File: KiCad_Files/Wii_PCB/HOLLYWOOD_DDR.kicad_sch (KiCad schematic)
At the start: 1 part

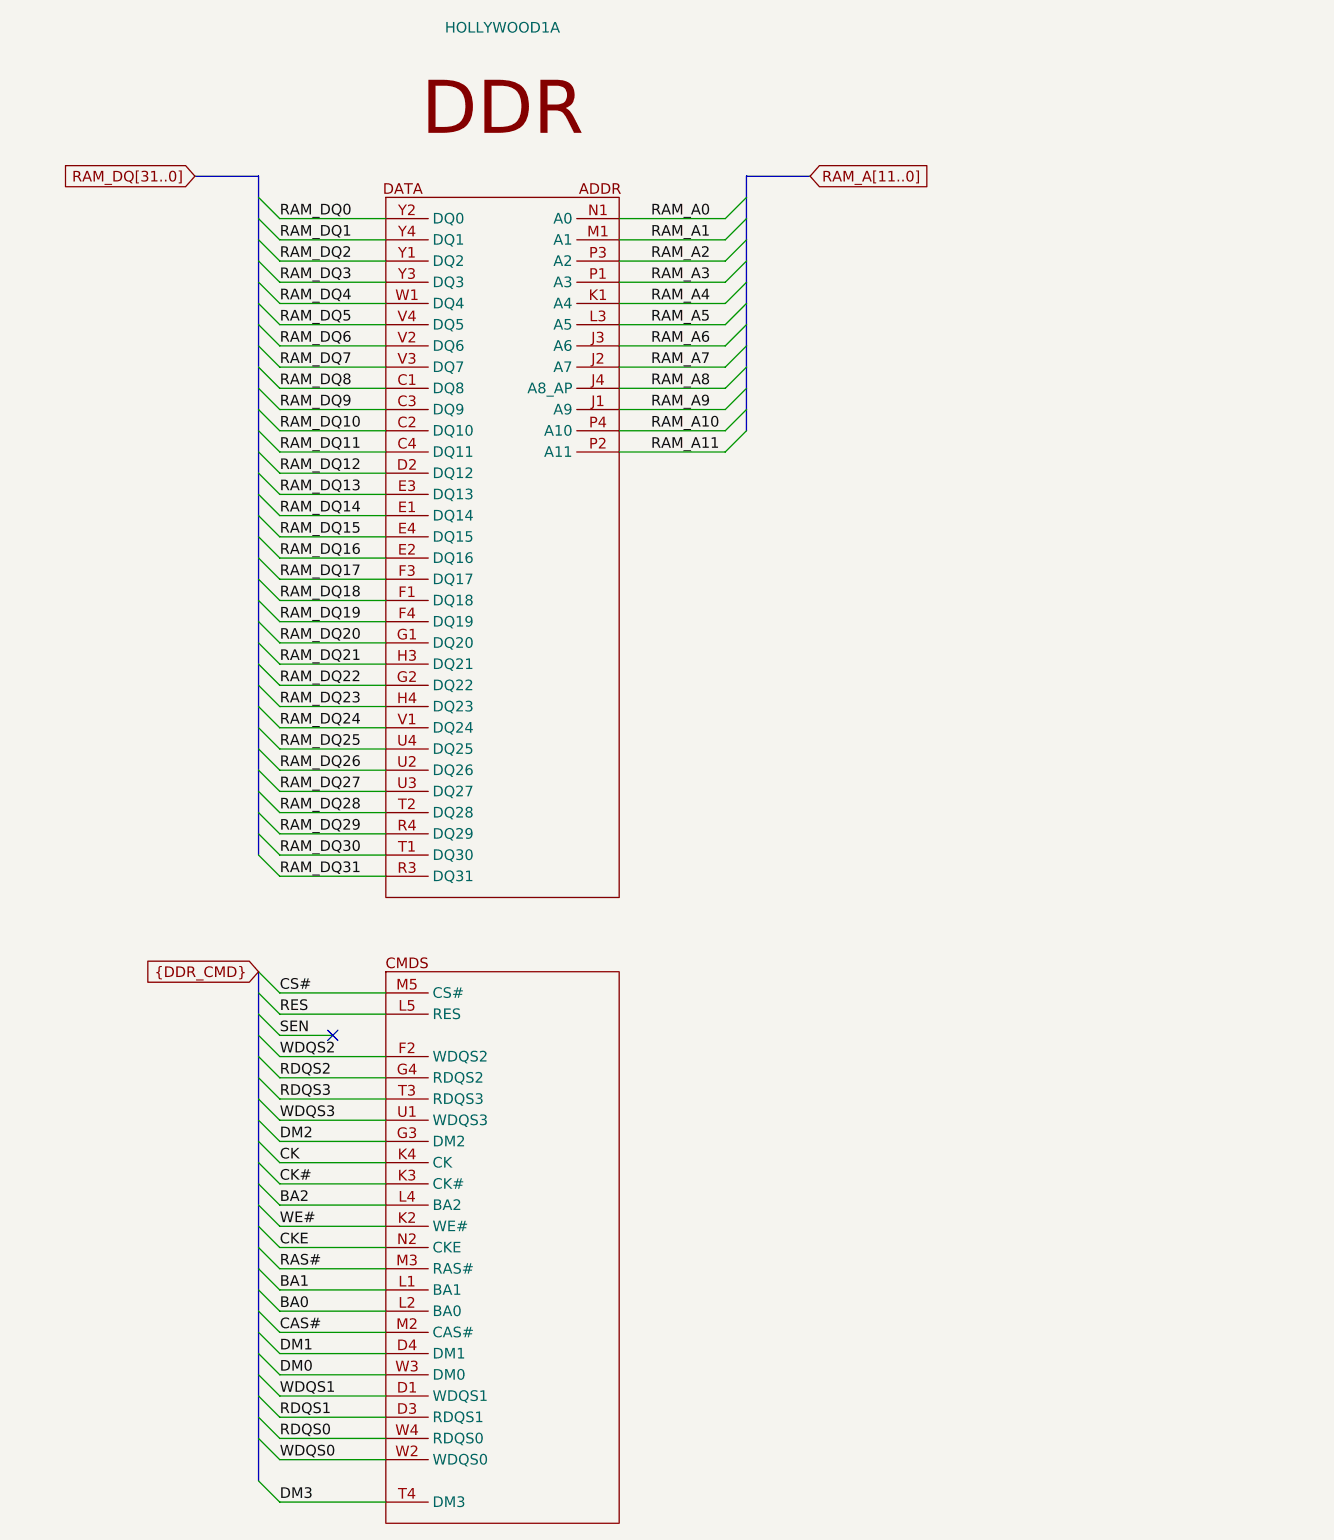
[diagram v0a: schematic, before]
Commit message: Updated RAM & GPU bus to allow custom net rules for measuring intra-track spacing, added pad for reset, removed debug pads, reorganized ram schematic to cluster length matched signals, changed MX chip and U10 symbols, and re-labeled the wifi net interface.
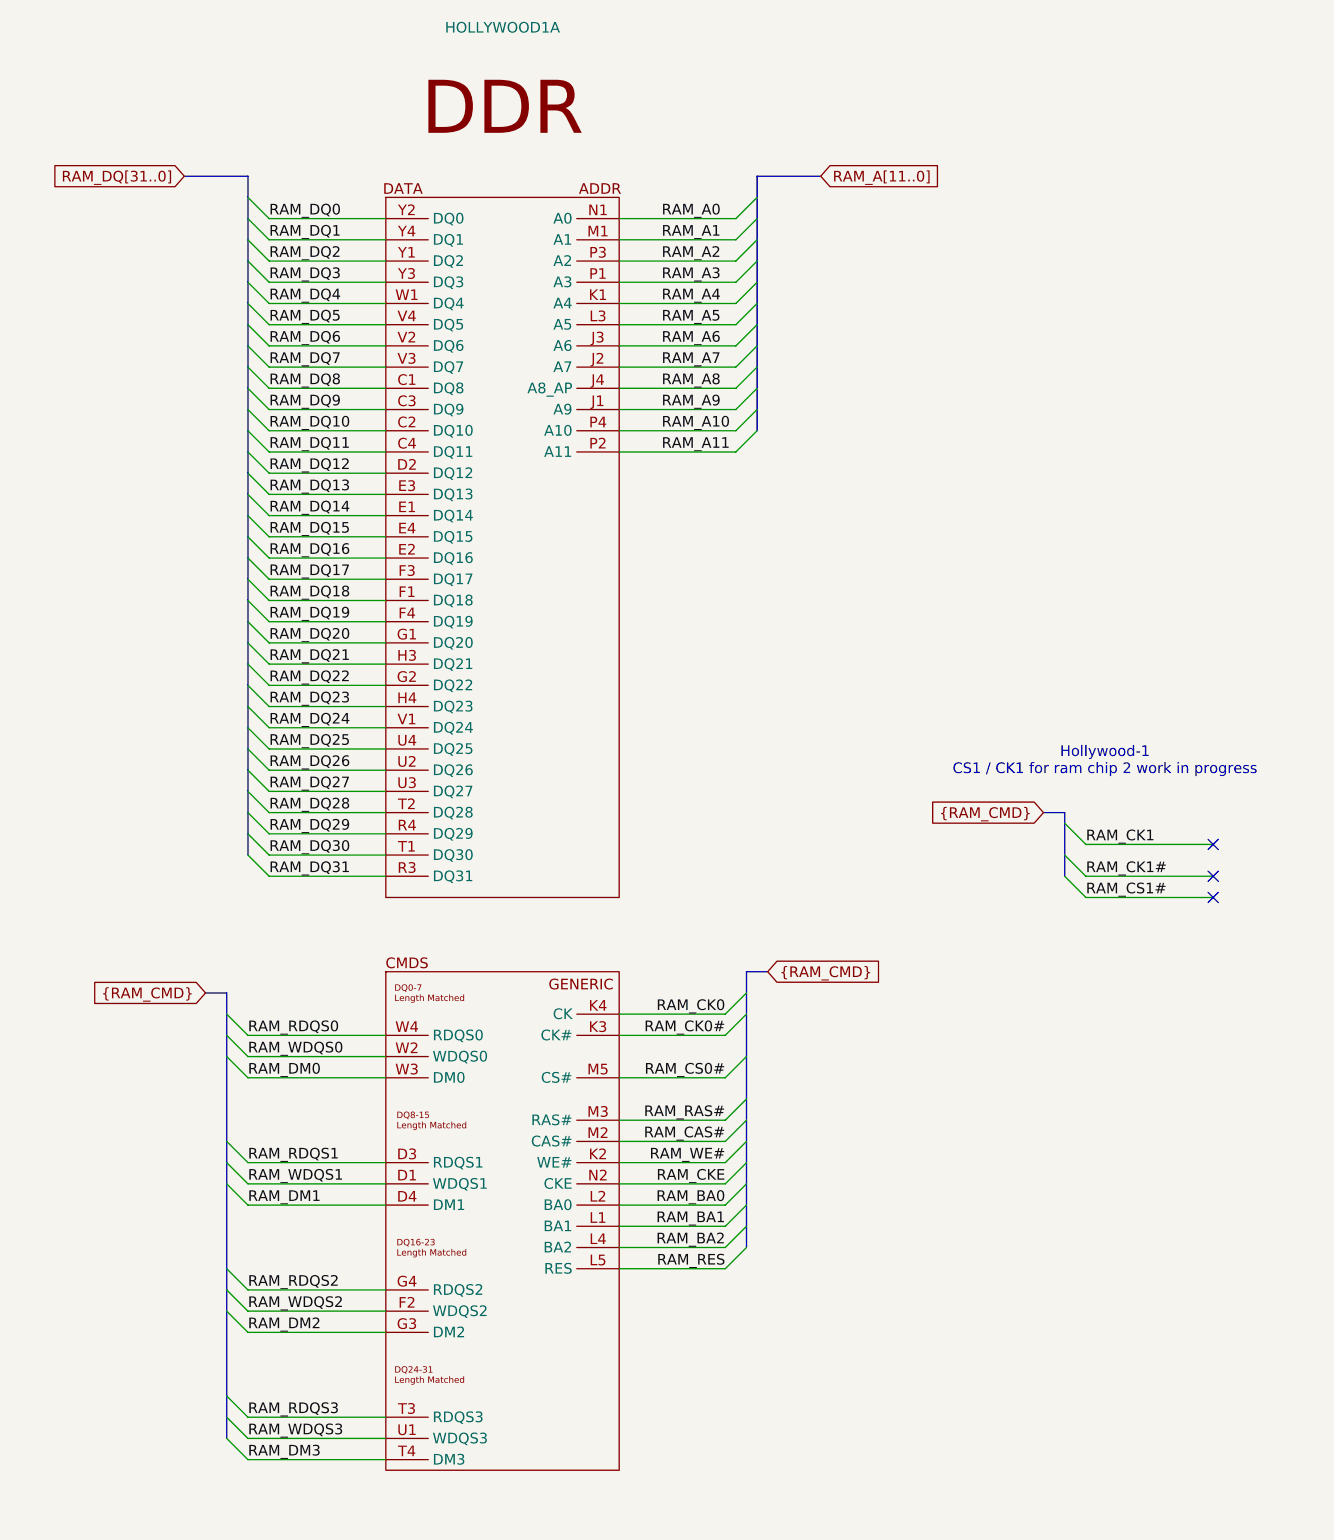
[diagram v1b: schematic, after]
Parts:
- HOLLYWOOD1: footprint wii_bgaLibrary:Updated HOLLYWOOD -> WeeWii_Library:Updated HOLLYWOOD
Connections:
- net BA0 renamed RAM_BA0
- net BA1 renamed RAM_BA1
- net BA2 renamed RAM_BA2
- net CAS# renamed RAM_CAS#
- net CK renamed RAM_CK0
- net CK# renamed RAM_CK0#
- net CKE renamed RAM_CKE
- net CS# renamed RAM_CS0#
- net DM0 renamed RAM_DM0
- net DM1 renamed RAM_DM1
- net DM2 renamed RAM_DM2
- net DM3 renamed RAM_DM3
- net RAS# renamed RAM_RAS#
- net RDQS0 renamed RAM_RDQS0
- net RDQS1 renamed RAM_RDQS1
- net RDQS2 renamed RAM_RDQS2
- net RDQS3 renamed RAM_RDQS3
- net RES renamed RAM_RES
- net WDQS0 renamed RAM_WDQS0
- net WDQS1 renamed RAM_WDQS1
- net WDQS2 renamed RAM_WDQS2
- net WDQS3 renamed RAM_WDQS3
- net WE# renamed RAM_WE#
- no-connect marks 1 -> 3
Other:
- note added: "Hollywood-1 CS1 / CK1 for ram chip 2 work in progress"
